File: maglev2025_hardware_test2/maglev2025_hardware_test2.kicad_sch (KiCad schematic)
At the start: 105 parts, among them J1 SWD, J2 PWRIn, U1 RY8411, U10 INA240A1PW, U11 INA240A1PW, U12 INA240A1PW, U2 TMAG5170-Q1, U3 STM32G474RBTx, U4 RS3236, U5 AT8236, U6 AT8236, U7 AT8236, U8 AT8236, U9 INA240A1PW, Y1 25MHz

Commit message: finish test2 sche
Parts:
- added BZ1: Buzzer, 0_RM2024:MLT-9032, symbol Device:Buzzer
- added C58, C62: 100u 16V, Capacitor_THT:CP_Radial_D6.3mm_P2.50mm, symbol Device:C_Polarized
- added C59, C63, C64: 10u, Capacitor_SMD:C_1206_3216Metric, symbol Device:C_Small
- added C60, C67, C68, C69, C70, C71, C72, C73, C74, C75, C76, C77, C78, C79, C80, C81: 100n, Capacitor_SMD:C_0603_1608Metric, symbol Device:C_Small
- added C61: 10n, Capacitor_SMD:C_0603_1608Metric, symbol Device:C_Small
- added C65: 10u, Capacitor_SMD:C_0603_1608Metric, symbol Device:C
- added C66: 20p, Capacitor_SMD:C_0603_1608Metric, symbol Device:C
- added D10, D12, D13, D14, D15, D16, D17, D18, D19, D20, D21, D6, D7, D8, D9: WS2812B, LED_SMD:LED_WS2812B_PLCC4_5.0x5.0mm_P3.2mm, symbol LED:WS2812B
- added D11: DSS34, Diode_SMD:D_SMF, symbol Device:D
- added D5: DSS34, symbol Device:D_Schottky
- added L6: 15u, Inductor_SMD:L_Sunlord_MWSA0402S, symbol Device:L
- added Q1: AO3400A, Package_TO_SOT_SMD:SOT-23, symbol Transistor_FET:AO3400A
- added R33: 3.24k, Resistor_SMD:R_0603_1608Metric, symbol Device:R_Small
- added R34: 10k, Resistor_SMD:R_0603_1608Metric, symbol Device:R
- added R35: 33r, Resistor_SMD:R_0603_1608Metric, symbol Device:R
- added R36: 33R, Resistor_SMD:R_0603_1608Metric, symbol Device:R_Small
- added R6: 10k, Resistor_SMD:R_0603_1608Metric, symbol Device:R_Small
- added U13: TPS5430DDA, Package_SO:TI_SO-PowerPAD-8_ThermalVias, symbol Regulator_Switching:TPS5430DDA
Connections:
- net 5V: now also BZ1.2 (+), C65.1, C66.1, D11.1 (K)
- net GND: now also C58.2, C59.2, C60.2, C62.2, C63.2, C64.2, C65.2, C67.2, C68.2, C69.2, C70.2, C71.2, C72.2, C73.2, C74.2, C75.2, C76.2, C77.2, C78.2, C79.2, C80.2, C81.2, D10.3 (VSS), D12.3 (VSS), D13.3 (VSS), D14.3 (VSS), D15.3 (VSS), D16.3 (VSS), D17.3 (VSS), D18.3 (VSS), D19.3 (VSS), D20.3 (VSS), D21.3 (VSS), D5.2 (A), D6.3 (VSS), D7.3 (VSS), D8.3 (VSS), D9.3 (VSS), Q1.2 (S), R33.2, R34.1, U13.6 (GND), U13.9 (GNDPAD)
- net VPP: now also C58.1, C59.1, C60.1, U13.7 (VIN)
- net PC13: now reaches U3.2 (PC13)
- net PC14: now reaches U3.3 (PC14)
- net PC15: now reaches U3.4 (PC15)
- net PD2: now reaches U3.55 (PD2)
- net PB3: now reaches U3.56 (PB3)
- net PB3: now also R36.1
- net BUZZER: now reaches U3.8 (PC0)
- net BUZZER: now also R34.2, R35.1
- new net: D14.2 (DOUT), D15.4 (DIN)
- new net: D13.2 (DOUT), D14.4 (DIN)
- new net: D16.2 (DOUT), D17.4 (DIN)
- new net: D15.2 (DOUT), D16.4 (DIN)
- new net: BZ1.1 (-), C66.2, D11.2 (A), Q1.3 (D)
- new net: C61.1, U13.1 (BOOT)
- new net: C61.2, D5.1 (K), L6.1, U13.8 (PH)
- new net: D6.2 (DOUT), D7.4 (DIN)
- new net: D6.4 (DIN), R36.2
- new net: Q1.1 (G), R35.2
- new net: D20.2 (DOUT), D21.4 (DIN)
- new net: D19.2 (DOUT), D20.4 (DIN)
- new net: D8.2 (DOUT), D9.4 (DIN)
- new net: D7.2 (DOUT), D8.4 (DIN)
- new net: D12.2 (DOUT), D13.4 (DIN)
- new net: D10.2 (DOUT), D12.4 (DIN)
- new net: D10.4 (DIN), D9.2 (DOUT)
- new net: D18.2 (DOUT), D19.4 (DIN)
- new net: D17.2 (DOUT), D18.4 (DIN)
- new net +5V_BLINK: C62.1, C63.1, C64.1, C67.1, C68.1, C69.1, C70.1, C71.1, C72.1, C73.1, C74.1, C75.1, C76.1, C77.1, C78.1, C79.1, C80.1, C81.1, D10.1 (VDD), D12.1 (VDD), D13.1 (VDD), D14.1 (VDD), D15.1 (VDD), D16.1 (VDD), D17.1 (VDD), D18.1 (VDD), D19.1 (VDD), D20.1 (VDD), D21.1 (VDD), D6.1 (VDD), D7.1 (VDD), D8.1 (VDD), D9.1 (VDD), L6.2, R6.1
- new net VSENSE: R33.1, R6.2, U13.4 (VSENSE)
- no-connect marks 15 -> 12
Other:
- note added: "WS2812"
- moved on the sheet: C13, C15, C35, C36, C37, C38, C51, H1, H2, H3, H4, H5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

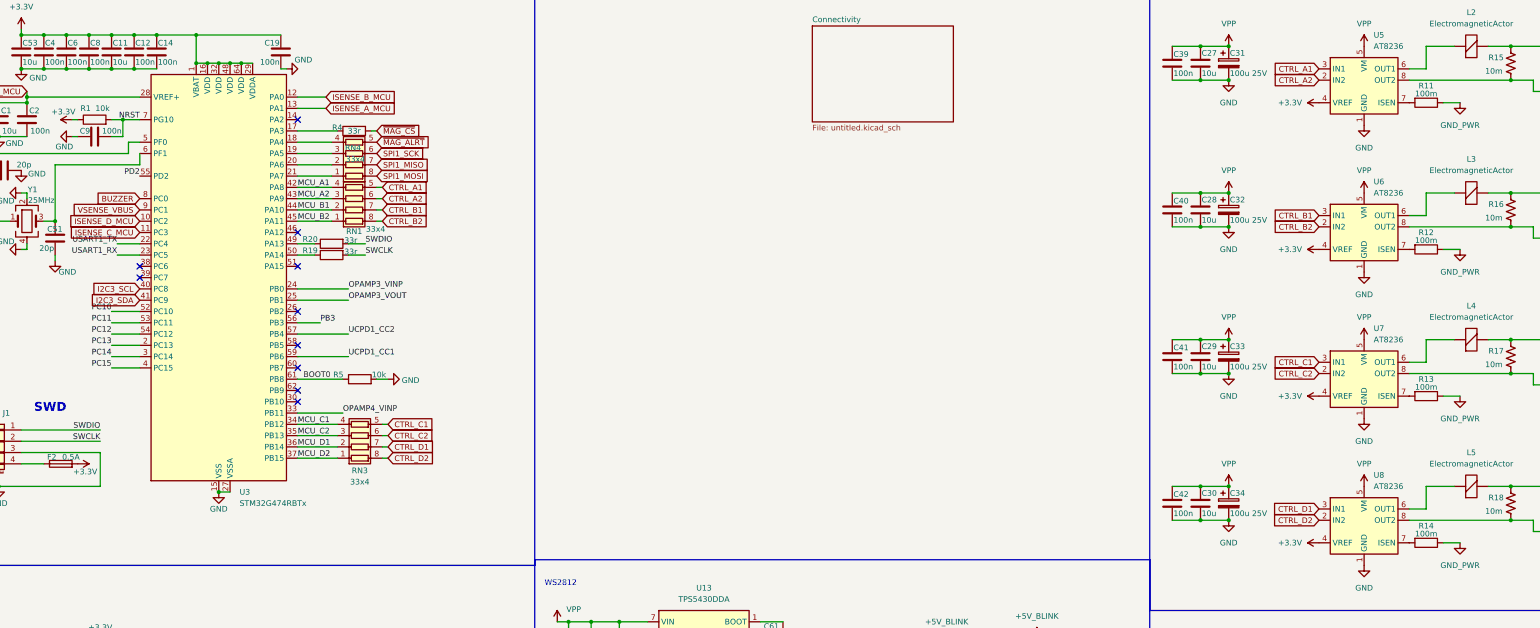
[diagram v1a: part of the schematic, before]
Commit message: Fix on test 2 schematic
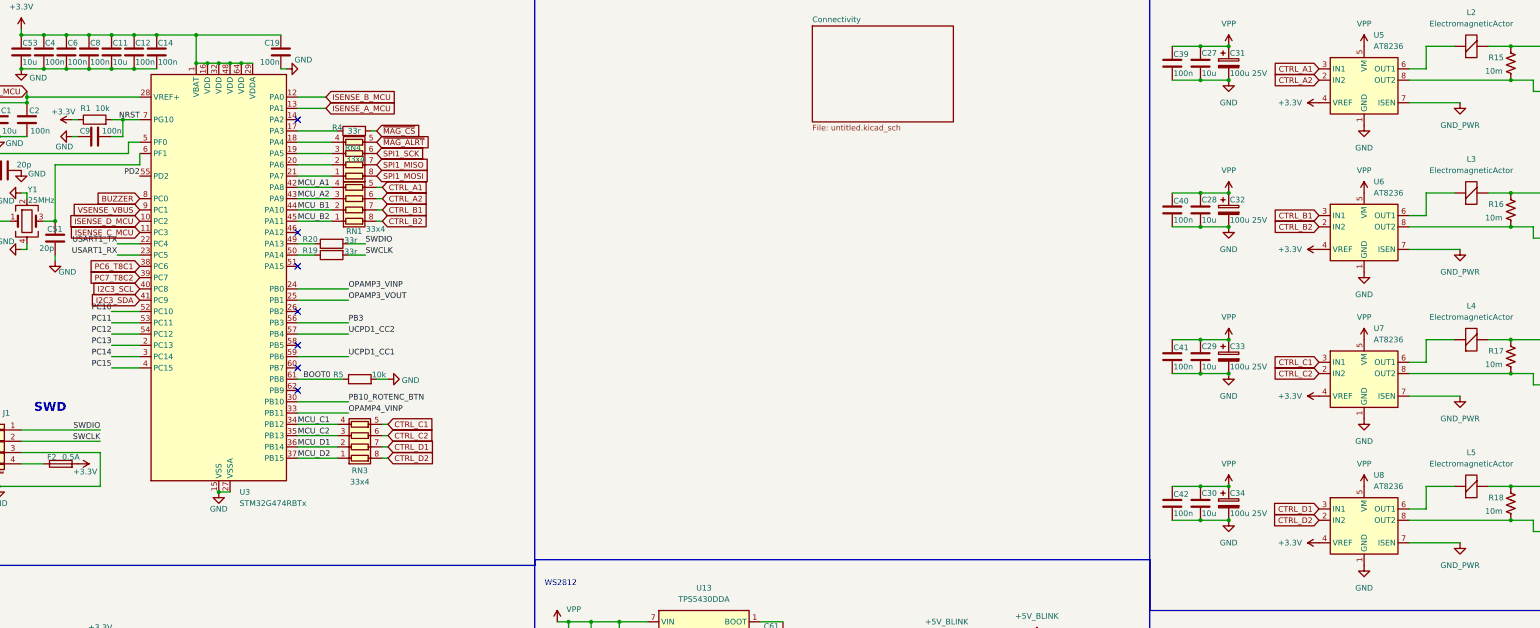
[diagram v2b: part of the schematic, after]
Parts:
- removed R11, R12, R13, R14: 100m, Resistor_SMD:R_2512_6332Metric, symbol Device:R
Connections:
- net GND_PWR: now also U5.7 (ISEN), U6.7 (ISEN), U7.7 (ISEN), U8.7 (ISEN)
- net PB10_ROTENC_BTN: now reaches U3.30 (PB10)
- net PC6_T8C1: now reaches U3.38 (PC6)
- net PC7_T8C2: now reaches U3.39 (PC7)
- no-connect marks 12 -> 9

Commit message: start layout
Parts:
- BZ1: footprint 0_RM2024:MLT-9032 -> RM25:MLT-9032
- D5: footprint (none) -> Diode_SMD:D_SMA
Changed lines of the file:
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@@
 			)
 		)
-		(property "Footprint" "0_RM2024:MLT-9032"
+		(property "Footprint" "RM25:MLT-9032"
 			(at 99.695 176.53 90)
 			(effects
@@
 			)
 		)
-		(property "Footprint" ""
+		(property "Footprint" "Diode_SMD:D_SMA"
 			(at 204.47 166.37 0)
 			(effects

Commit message: addjust layout
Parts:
- removed C80: 100n, Capacitor_SMD:C_0603_1608Metric, symbol Device:C_Small
- removed D21: WS2812B, LED_SMD:LED_WS2812B_PLCC4_5.0x5.0mm_P3.2mm, symbol LED:WS2812B
- added C55, C85, C86, C87, C88: 100n, Capacitor_SMD:C_0603_1608Metric, symbol Device:C
- added C57: 10n, Capacitor_SMD:C_0603_1608Metric, symbol Device:C
- added D4: DK5V45R10, Diode_SMD:D_PowerDI-5, symbol Device:D
- added F3: 5A, Fuse:Fuse_1206_3216Metric, symbol Device:Fuse
- added J3, J6: Conn_01x04, Connector_PinHeader_2.54mm:PinHeader_1x04_P2.54mm_Vertical, symbol Connector_Generic:Conn_01x04
- added J4: Conn_01x04_MountingPin, Connector_JST:JST_GH_BM04B-GHS-TBT_1x04-1MP_P1.25mm_Vertical, symbol Connector_Generic_MountingPin:Conn_01x04_MountingPin
- added J5: USB_C_Receptacle_USB2.0, Connector_USB:USB_C_Receptacle_HRO_TYPE-C-31-M-12, symbol Connector:USB_C_Receptacle_USB2.0
- added R21, R22, R25, R26, R28, R29, R37, R38, R39, R40: 33r, Resistor_SMD:R_0603_1608Metric, symbol Device:R
- added R23, R24: 4.7k, Resistor_SMD:R_0603_1608Metric, symbol Device:R
- added R27: 1M, Resistor_SMD:R_0603_1608Metric, symbol Device:R
- added R30: R_US, Resistor_SMD:R_2512_6332Metric, symbol Device:R_US
- added R31, R50, R52, R55: 10k, Resistor_SMD:R_0603_1608Metric, symbol Device:R
- added R32: 1k, Resistor_SMD:R_0603_1608Metric, symbol Device:R
- added R41, R42: 5.1k, Resistor_SMD:R_0603_1608Metric, symbol Device:R
- added R51, R53, R54: 33, Resistor_SMD:R_0603_1608Metric, symbol Device:R
- added SW4: RotaryEncoder_Switch_MP, Rotary_Encoder:RotaryEncoder_Alps_EC11E-Switch_Vertical_H20mm_MountingHoles, symbol Device:RotaryEncoder_Switch_MP
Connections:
- net OPAMP4_VINP is gone; now on net GND_PWR: U3.33 (PB11)
- net +3.3V: now also J3.2 (Pin_2), R23.2, R24.2, R50.1, R52.1, R55.1
- net GND: now also C55.2, C57.2, C85.1, C86.1, C87.1, C88.1, J3.1 (Pin_1), J4.4 (Pin_4), J4.MP (MountPin), J5.A1 (GND), J5.A12 (GND), J5.B1 (GND), J5.B12 (GND), R27.2, R30.2, R32.1, R41.1, R42.1, SW4.C, SW4.MP, SW4.S2; no longer U5.1 (GND), U5.9 (GND), U6.1 (GND), U6.9 (GND), U7.1 (GND), U7.9 (GND), U8.1 (GND), U8.9 (GND)
- net GND_PWR: now also U5.1 (GND), U5.9 (GND), U6.1 (GND), U6.9 (GND), U7.1 (GND), U7.9 (GND), U8.1 (GND), U8.9 (GND), R30.1
- net I2C3_SCL: now also R22.2, R24.1
- net I2C3_SDA: now also R23.1, R25.2
- net PB10_ROTENC_BTN: now also C85.2, R51.1
- net PC10: now also R38.1
- net PC11: now also R39.1
- net PC12: now also R40.1
- net PC6_T8C1: now also C86.2, R53.1
- net PC7_T8C2: now also C87.2, R54.1
- net PD2: now also R37.1
- net UCPD1_CC1: now also R28.2, R41.2
- net UCPD1_CC2: now also R29.2, R42.2
- net USART1_RX: now also R21.1
- net USART1_TX: now also R26.1
- net VPP: now also D4.1 (K), R31.2
- net VSENSE_VBUS: now also C88.2, R31.1, R32.2
- new net: J3.3 (Pin_3), R22.1
- new net: J3.4 (Pin_4), R25.1
- new net: F3.1, J5.A4 (VBUS), J5.A9 (VBUS), J5.B4 (VBUS), J5.B9 (VBUS)
- new net: J5.A5 (CC1), R28.1
- new net: J5.B5 (CC2), R29.1
- new net: C57.1, J5.S1 (SHIELD), R27.1
- new net: R50.2, R51.2, SW4.S1
- new net: R52.2, R53.2, SW4.A
- new net: R54.2, R55.2, SW4.B
- new net: J6.1 (Pin_1), R37.2
- new net: J6.2 (Pin_2), R38.2
- new net: J6.3 (Pin_3), R39.2
- new net: J6.4 (Pin_4), R40.2
- new net: J4.1 (Pin_1), R21.2
- new net: J4.2 (Pin_2), R26.2
- new net: D4.2 (A), F3.2
- new net +5V: C55.1, J4.3 (Pin_3)
- no-connect marks 9 -> 15
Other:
- note added: "EXTEND GPIO"
- note added: "I2C OLED Display"
- note added: "UART"
- note added: "UCPD"

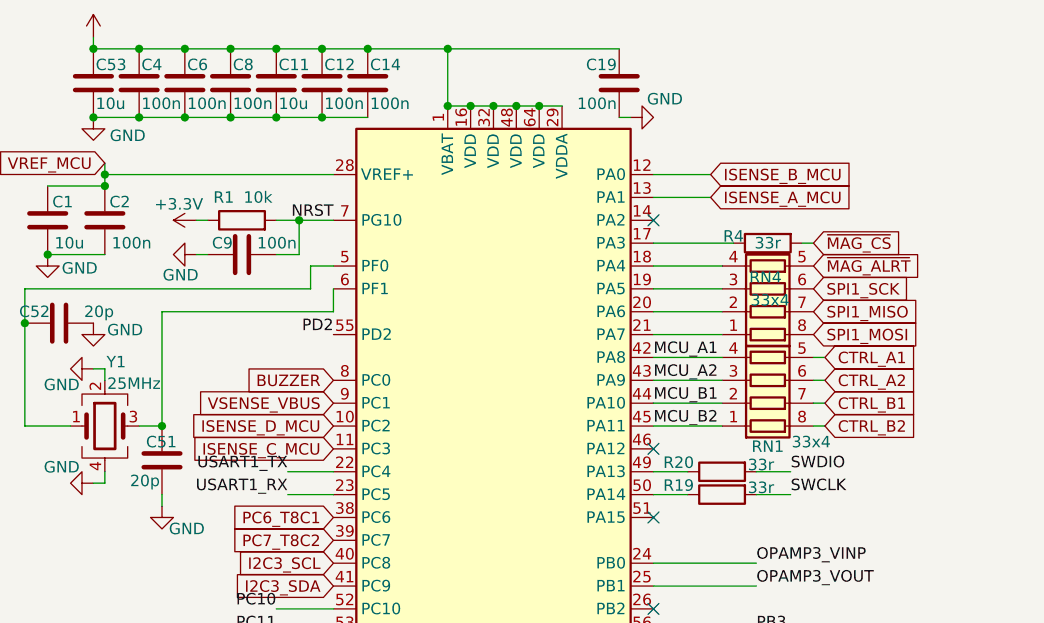
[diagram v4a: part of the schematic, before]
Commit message: change adc pin out
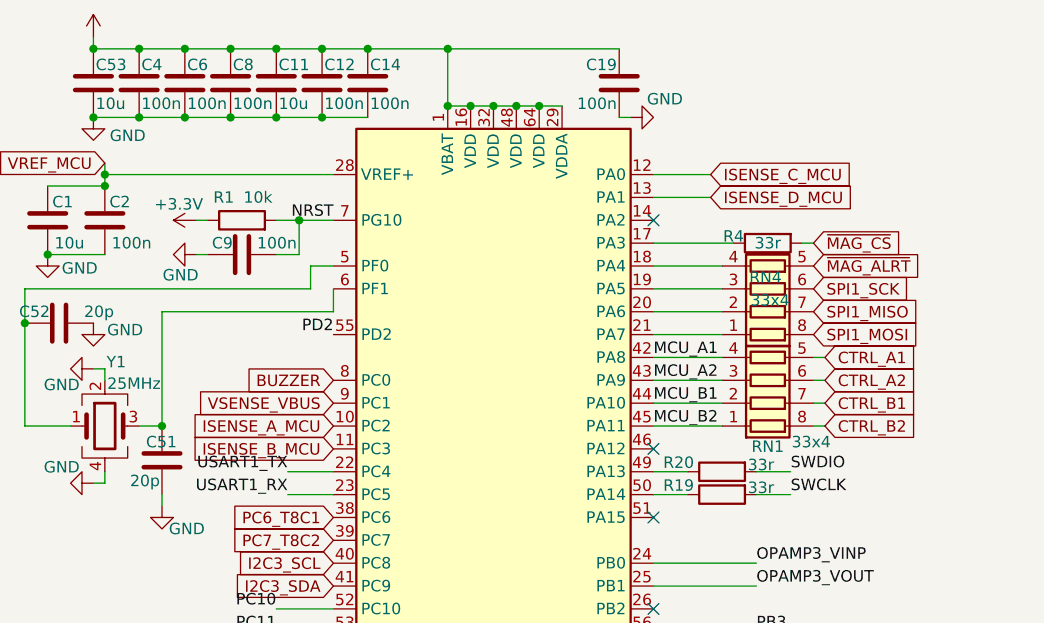
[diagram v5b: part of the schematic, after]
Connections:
- net ISENSE_A_MCU: now also U3.10 (PC2); no longer U3.13 (PA1)
- net ISENSE_B_MCU: now also U3.11 (PC3); no longer U3.12 (PA0)
- net ISENSE_C_MCU: now also U3.12 (PA0); no longer U3.11 (PC3)
- net ISENSE_D_MCU: now also U3.13 (PA1); no longer U3.10 (PC2)
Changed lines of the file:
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@@
-		)
-	)
-	(global_label "ISENSE_B_MCU"
-		(shape input)
-		(at 93.98 38.1 0)
-		(fields_autoplaced yes)
-		(effects
-			(font
-				(size 1.27 1.27)
-			)
-			(justify left)
-		)
-		(property "Intersheetrefs" "${INTERSHEET_REFS}"
-			(at 110.8746 38.1 0)
-			(effects
-				(font
-					(size 1.27 1.27)
-				)
-				(justify left)
-				(hide yes)
-			)
 		)
 	)
@@
 		)
 	)
-	(global_label "ISENSE_D_MCU"
-		(shape input)
-		(at 52.07 66.04 180)
-		(fields_autoplaced yes)
-		(effects
-			(font
-				(size 1.27 1.27)
-			)
-			(justify right)
-		)
-		(property "Intersheetrefs" "${INTERSHEET_REFS}"
-			(at 35.1754 66.04 0)
-			(effects
-				(font
-					(size 1.27 1.27)
-				)
-				(justify right)
-				(hide yes)
-			)
-		)
-	)
 	(global_label "PC6_T8C1"
 		(shape input)
@@
 		)
 	)
+	(global_label "ISENSE_D_MCU"
+		(shape input)
+		(at 93.98 40.64 0)
+		(fields_autoplaced yes)
+		(effects
+			(font
+				(size 1.27 1.27)
+			)
+			(justify left)
+		)
+		(property "Intersheetrefs" "${INTERSHEET_REFS}"
+			(at 110.8746 40.64 0)
+			(effects
+				(font
+					(size 1.27 1.27)
+				)
+				(justify left)
+				(hide yes)
+			)
+		)
+	)
 	(global_label "VREF"
 		(shape input)
@@
 		)
 	)
+	(global_label "ISENSE_C_MCU"
+		(shape input)
+		(at 93.98 38.1 0)
+		(fields_autoplaced yes)
+		(effects
+			(font
+				(size 1.27 1.27)
+			)
+			(justify left)
+		)
+		(property "Intersheetrefs" "${INTERSHEET_REFS}"
+			(at 110.8746 38.1 0)
+			(effects
+				(font
+					(size 1.27 1.27)
+				)
+				(justify left)
+				(hide yes)
+			)
+		)
+	)
 	(global_label "VREF"
 		(shape input)
@@
 				)
 				(justify left)
+				(hide yes)
+			)
+		)
+	)
+	(global_label "ISENSE_B_MCU"
+		(shape input)
+		(at 52.07 68.58 180)
+		(fields_autoplaced yes)
+		(effects
+			(font
+				(size 1.27 1.27)
+			)
+			(justify right)
+		)
+		(property "Intersheetrefs" "${INTERSHEET_REFS}"
+			(at 35.1754 68.58 0)
+			(effects
+				(font
+					(size 1.27 1.27)
+				)
+				(justify right)
 				(hide yes)
 			)
@@
 		)
 	)
-	(global_label "ISENSE_C_MCU"
-		(shape input)
-		(at 52.07 68.58 180)
-		(fields_autoplaced yes)
-		(effects
-			(font
-				(size 1.27 1.27)
-			)
-			(justify right)
-		)
-		(property "Intersheetrefs" "${INTERSHEET_REFS}"
-			(at 35.1754 68.58 0)
+	(global_label "ISENSE_A_MCU"
+		(shape input)
+		(at 52.07 66.04 180)
+		(fields_autoplaced yes)
+		(effects
+			(font
+				(size 1.27 1.27)
+			)
+			(justify right)
+		)
+		(property "Intersheetrefs" "${INTERSHEET_REFS}"
+			(at 35.3568 66.04 0)
 			(effects
 				(font
@@
 			(effects
 				(font
-					(size 1.27 1.27)
-				)
-				(justify left)
-				(hide yes)
-			)
-		)
-	)
-	(global_label "ISENSE_A_MCU"
-		(shape input)
-		(at 93.98 40.64 0)
-		(fields_autoplaced yes)
-		(effects
-			(font
-				(size 1.27 1.27)
-			)
-			(justify left)
-		)
-		(property "Intersheetrefs" "${INTERSHEET_REFS}"
-			(at 110.6932 40.64 0)
-			(effects
-				(font
